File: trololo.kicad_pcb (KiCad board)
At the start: 4 copper layers, 135.6 x 54.6 mm, 106 parts, among them J1 10118194-0001LF, J10 Conn_02x12_Odd_Even, J11 Conn_02x02_Odd_Even, J12 VBAT+, J13 PROTO1, J14 VBATG, J18 PROTO1, J2 10118194-0001LF, J3 RJ45_Amphenol_RJMG1BD3B8K1ANR, J4 Micro_SD_Card, J5 Screw_Terminal_01x06, J6 Conn_02x12_Odd_Even, J7 10118194-0001LF, J8 Screw_Terminal_01x02, J9 Conn_02x12_Odd_Even, SW1 RESET, SW2 PC13, U1 STM32H743VITx, U10 USBLC6-2SC6, U11 SN6505, U12 TCAN332, U13 ISL83483, U2 KSZ8081RNA, U3 ISO1050DUB, U4 ISO3082DW, U5 S25FL127SABMFI101, U6 AP63203, U7 USBLC6-2SC6, U8 STM32F042F6Px, U9 USBLC6-2SC6, Y1 8MHz, Y2 32.768KHz, Y3 25MHz

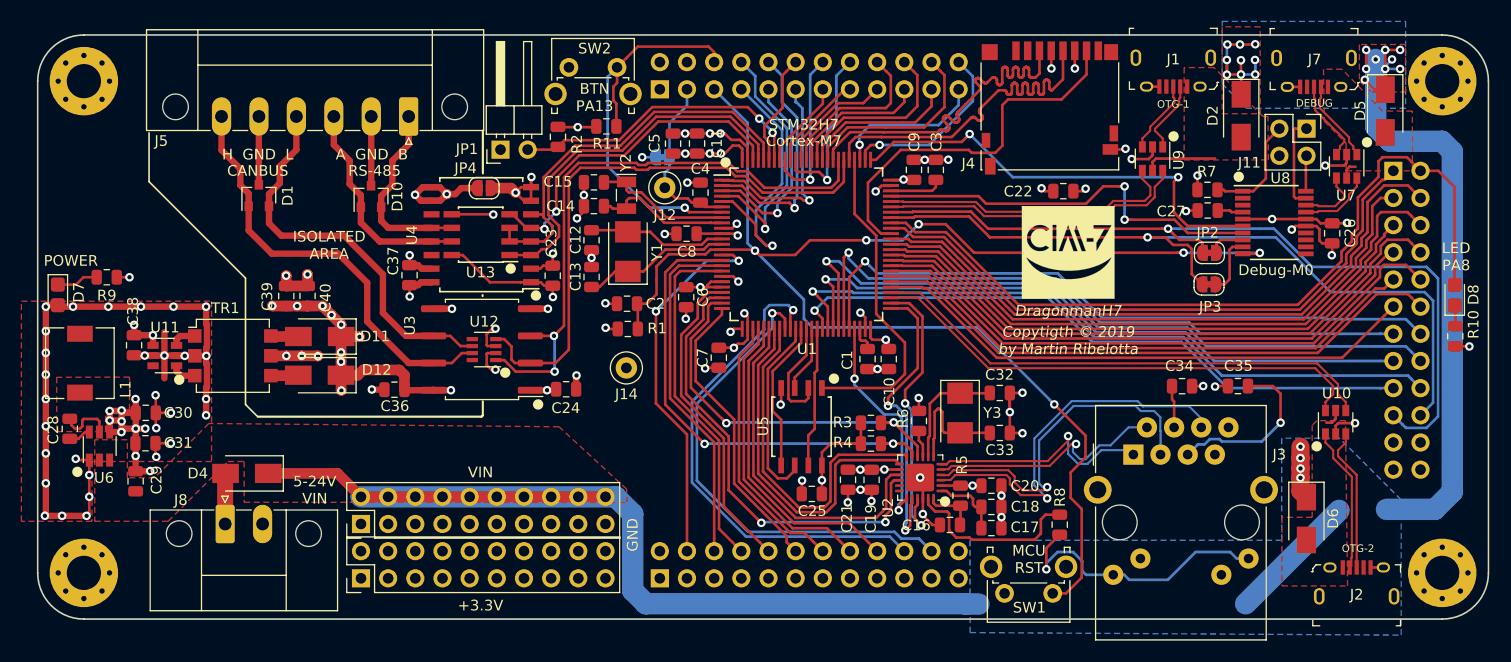
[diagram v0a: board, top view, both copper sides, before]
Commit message: Add patrocinator logo, silkscreen correctios and minor route changes
Signed-off-by: Martin Ribelotta <martinribelotta@gmail.com>
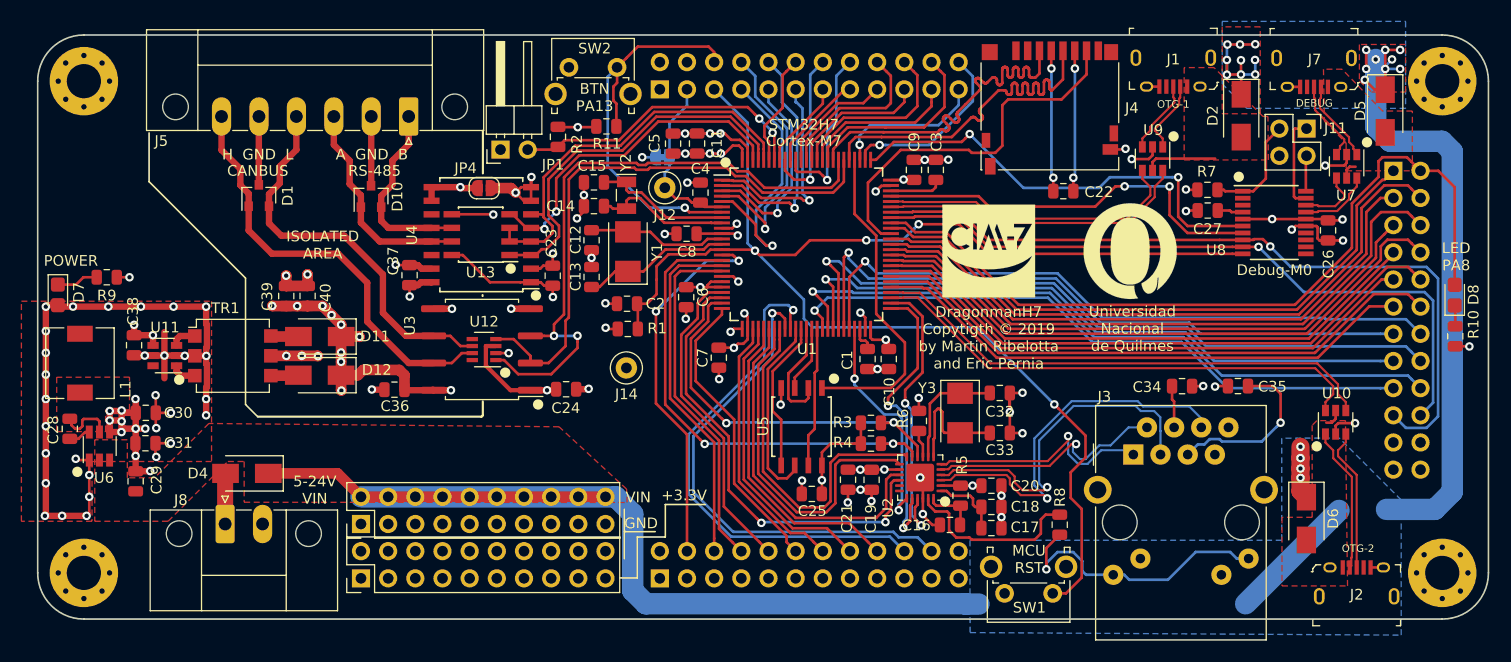
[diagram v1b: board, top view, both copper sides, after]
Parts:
- removed JP2, JP3: Jumper_2_Bridged, Jumper:SolderJumper-2_P1.3mm_Bridged_RoundedPad1.0x1.5mm
- added G***: LOGO, footprints:unqui-logo, F.Cu at (160.8, 48.3)
- moved G*** 7.43 mm to (147.6, 48.1)
- moved C26 0.47 mm to (179.3, 46.2)
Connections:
- U8 pad 8: /U2_TX -> /U1_RX
- U8 pad 9: /U2_RX -> /U1_TX
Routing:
- net +3V3: track 158.5 -> 173.0 mm, vias 54 -> 53
- net /U1_TX: track 73.5 -> 65.2 mm
- net GND: track 130.5 -> 138.6 mm
- net /U2_RX: track 5.58 -> 0.00 mm
- net /U1_RX: track 76.4 -> 71.8 mm
- net GNDPWR: track 37.4 -> 33.3 mm, vias 10 -> 9
- net /U2_TX: track 3.47 -> 0.00 mm
- net /CAN_TX: track 56.3 -> 59.5 mm
- net /~RESET: track 141.8 -> 138.6 mm, vias 6 -> 4
- net /PB1: track 46.4 -> 47.5 mm
- net /PB0: track 45.6 -> 46.7 mm
- net /CAN_RX: track 54.7 -> 54.0 mm
- net /PD11: track 56.4 -> 55.8 mm
- net /USBD_D+: track 27.9 -> 28.5 mm
- net /USBD_D-: track 28.6 -> 29.1 mm
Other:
- board text added: "DragonmanH7 Copytigth © 2019 by Martin Ribelotta and Eric Pernia"
- board text added: "Serial Number"
- board text added: "Universidad Nacional de Quilmes"
- board text removed: "Copytigth © 2019 by Martin Ribelotta"
- board text removed: "DragonmanH7"
